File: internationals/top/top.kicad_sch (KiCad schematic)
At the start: 19 parts, among them J1 Conn_01x08_Pin, J2 Pico-L-Headerx5, J3 Pico-Debug-Headerx3, J4 Pico-R-Headerx5, J5 Bottom-UART-XHx2, J6 IMU-UART-XHx2, J7 Conn_01x03_Pin, J8 IMU-I2C0-XHx2, J9 IMU-I2C1-XHx2, M1 MotorDriver1A-XH-B4B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

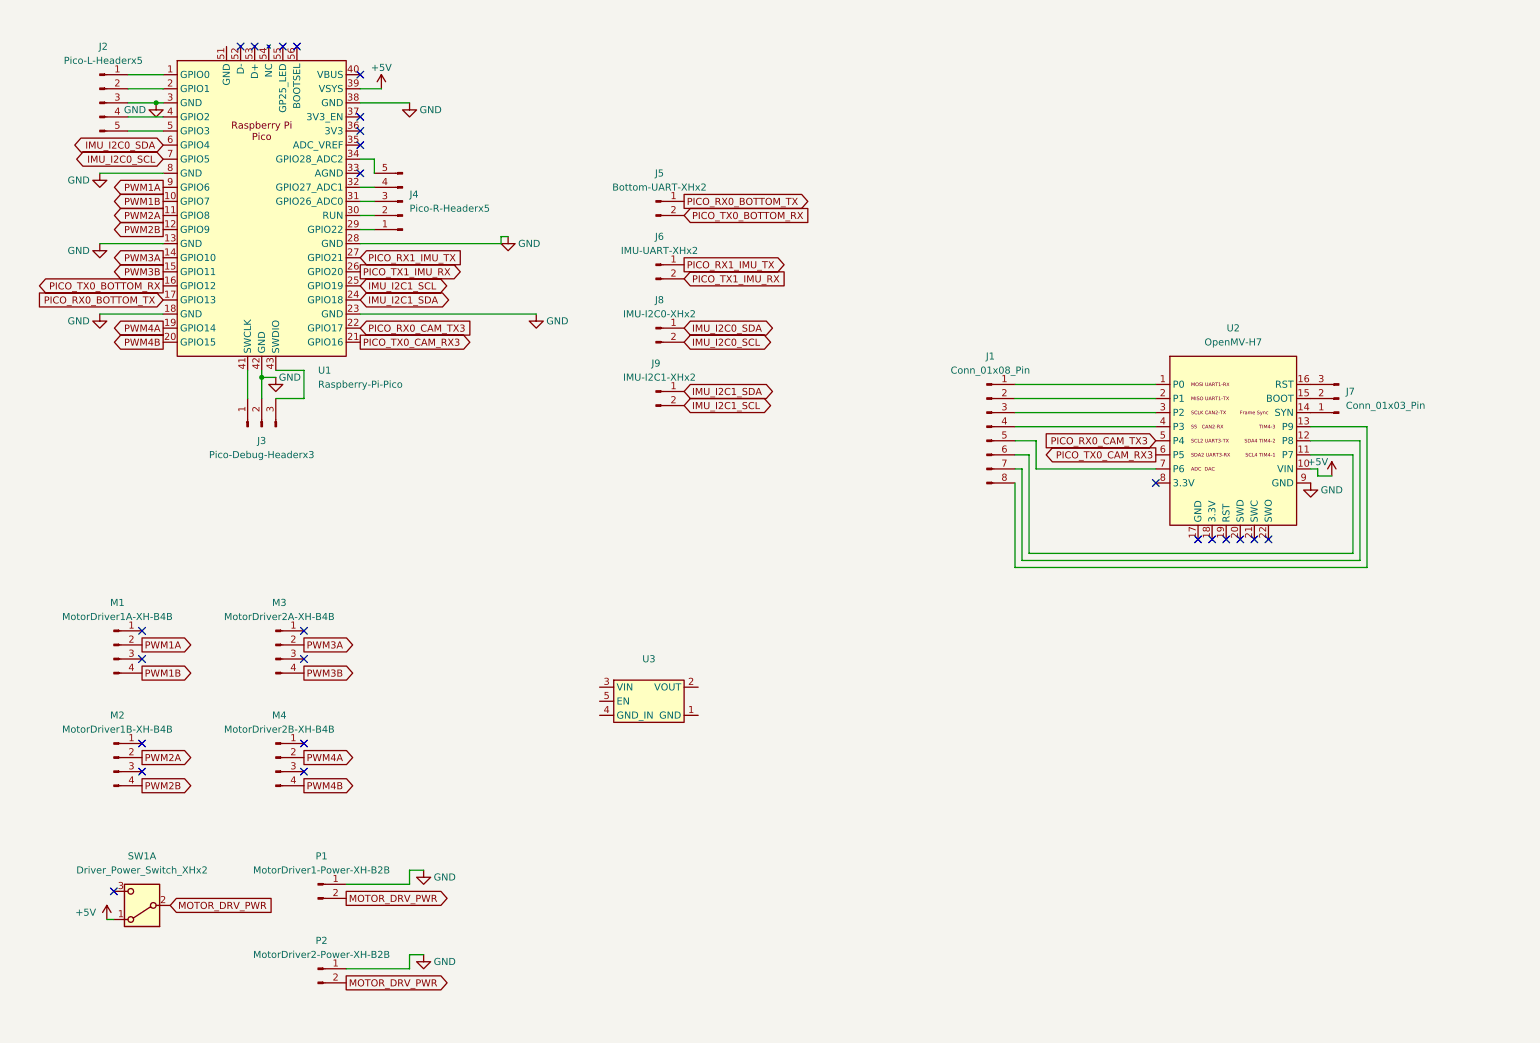
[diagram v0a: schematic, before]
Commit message: pcbs: top: feat: updated schematics
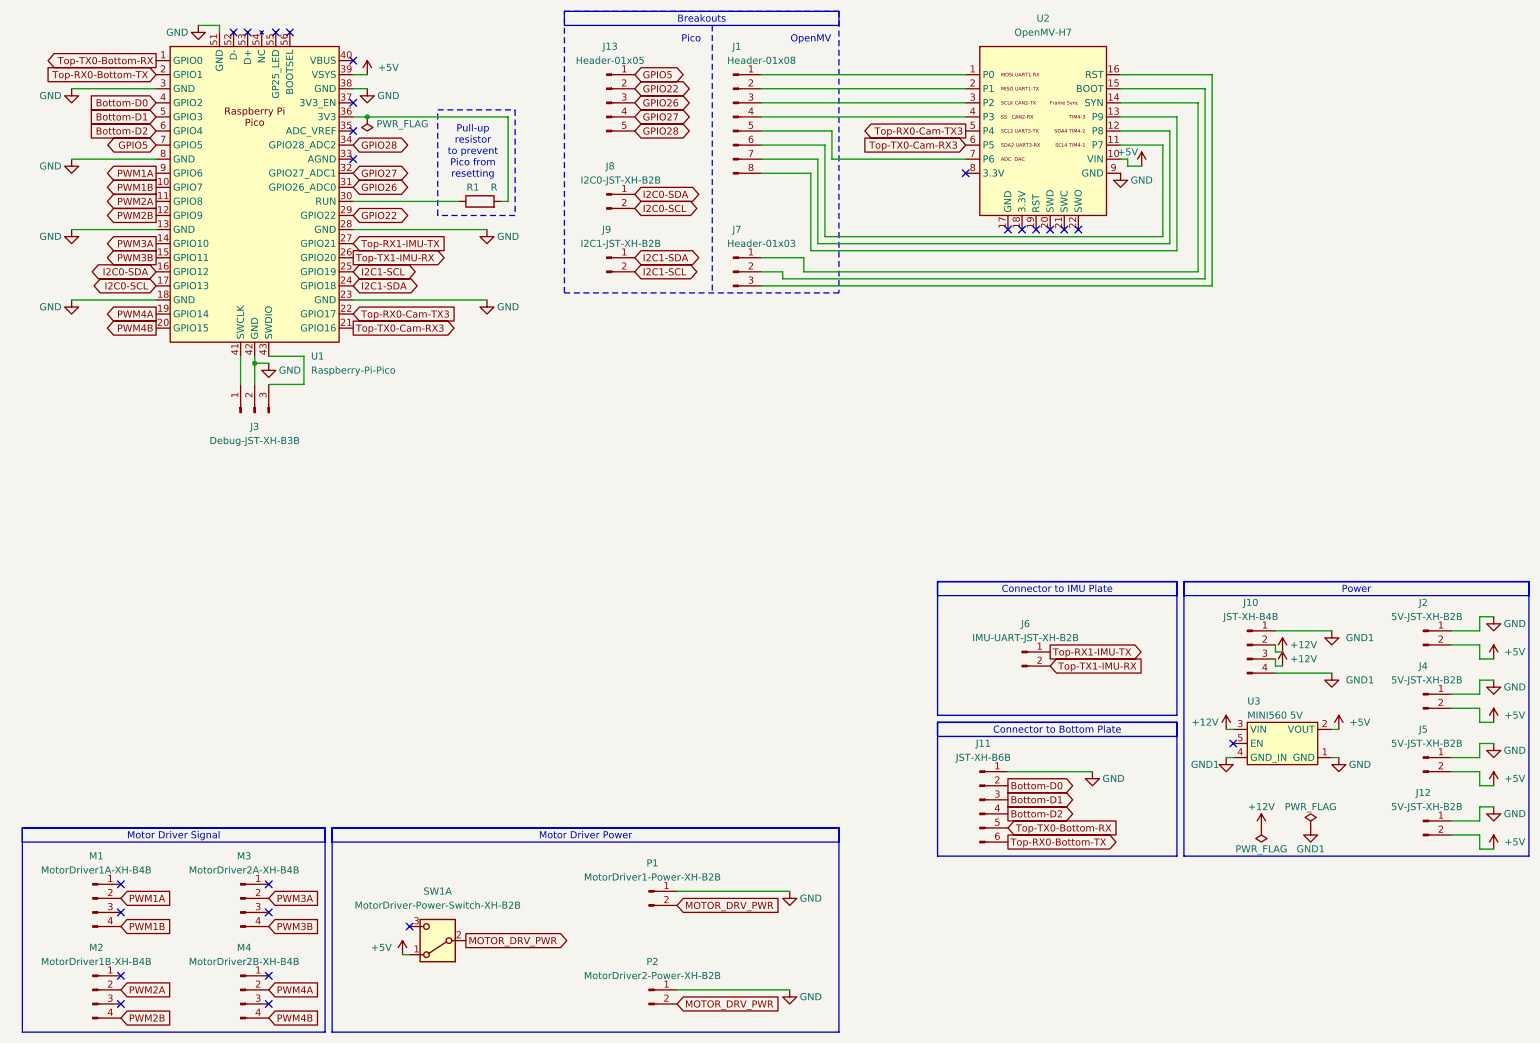
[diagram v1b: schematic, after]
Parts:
- removed J2: Pico-L-Headerx5, Connector_PinHeader_2.54mm:PinHeader_1x05_P2.54mm_Vertical, symbol Connector:Conn_01x05_Pin
- removed J4: Pico-R-Headerx5, Connector_PinHeader_2.54mm:PinHeader_1x05_P2.54mm_Vertical, symbol Connector:Conn_01x05_Pin
- added J10: JST-XH-B4B, Connector_JST:JST_XH_B4B-XH-A_1x04_P2.50mm_Vertical, symbol Connector:Conn_01x04_Pin
- added J11: JST-XH-B6B, Connector_JST:JST_XH_B6B-XH-A_1x06_P2.50mm_Vertical, symbol Connector:Conn_01x06_Pin
- added J12, J2, J4: 5V-JST-XH-B2B, Connector_JST:JST_XH_B2B-XH-A_1x02_P2.50mm_Vertical, symbol Connector:Conn_01x02_Pin
- added J13: Header-01x05, Connector_PinHeader_2.54mm:PinHeader_1x05_P2.54mm_Vertical, symbol Connector:Conn_01x05_Pin
- added R1: R, PCM_Resistor_THT_AKL:R_Axial_DIN0204_L3.6mm_D1.6mm_P5.08mm_Horizontal, symbol Device:R
- J1: value Conn_01x08_Pin -> Header-01x08; footprint (none) -> Connector_PinHeader_2.54mm:PinHeader_1x08_P2.54mm_Vertical
- J3: value Pico-Debug-Headerx3 -> Debug-JST-XH-B3B; footprint Connector_PinHeader_2.54mm:PinHeader_1x03_P2.54mm_Vertical -> Connector_JST:JST_XH_B3B-XH-A_1x03_P2.50mm_Vertical
- J5: value Bottom-UART-XHx2 -> 5V-JST-XH-B2B
- J6: value IMU-UART-XHx2 -> IMU-UART-JST-XH-B2B
- J7: value Conn_01x03_Pin -> Header-01x03; footprint (none) -> Connector_PinHeader_2.54mm:PinHeader_1x03_P2.54mm_Vertical
- J8: value IMU-I2C0-XHx2 -> I2C0-JST-XH-B2B
- J9: value IMU-I2C1-XHx2 -> I2C1-JST-XH-B2B
- SW1: value Driver_Power_Switch_XHx2 -> MotorDriver-Power-Switch-XH-B2B
- U3: value ~ -> MINI560 5V; footprint (none) -> PorridgePi-Personal:MINI560
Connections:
- net +5V: now also J5.2 (Pin_2), U3.2 (VOUT), J12.2 (Pin_2), J2.2 (Pin_2), J4.2 (Pin_2)
- net GND: now also J5.1 (Pin_1), U1.51 (GND), U3.1 (GND), J11.1 (Pin_1), J12.1 (Pin_1), J2.1 (Pin_1), J4.1 (Pin_1)
- net GPIO22: now reaches U1.29 (GPIO22)
- net GPIO22: now also J13.2 (Pin_2)
- net at U1.30 (RUN): now also R1.1
- net GPIO26: now reaches U1.31 (GPIO26_ADC0)
- net GPIO26: now also J13.3 (Pin_3)
- net GPIO27: now reaches U1.32 (GPIO27_ADC1)
- net GPIO27: now also J13.4 (Pin_4)
- net GPIO28: now reaches U1.34 (GPIO28_ADC2)
- net GPIO28: now also J13.5 (Pin_5)
- net +12V: now reaches U3.3 (VIN)
- net +12V: now also J10.2 (Pin_2), J10.3 (Pin_3)
- net GND1: now reaches U3.4 (GND_IN)
- net GND1: now also J10.1 (Pin_1), J10.4 (Pin_4)
- net Top-TX0-Bottom-RX: now reaches U1.1 (GPIO0)
- net Top-TX0-Bottom-RX: now also J11.5 (Pin_5)
- net Top-RX0-Bottom-TX: now reaches U1.2 (GPIO1)
- net Top-RX0-Bottom-TX: now also J11.6 (Pin_6)
- net at U1.36 (3V3): now also R1.2
- net Bottom-D0: now reaches U1.4 (GPIO2)
- net Bottom-D0: now also J11.2 (Pin_2)
- net Bottom-D1: now reaches U1.5 (GPIO3)
- net Bottom-D1: now also J11.3 (Pin_3)
- net IMU_I2C0_SCL renamed GPIO5
- net GPIO5: now also J13.1 (Pin_1); no longer J8.2 (Pin_2)
- net IMU_I2C0_SDA renamed Bottom-D2
- net Bottom-D2: now also J11.4 (Pin_4); no longer J8.1 (Pin_1)
- net IMU_I2C1_SCL renamed I2C1-SCL
- net IMU_I2C1_SDA renamed I2C1-SDA
- net PICO_RX0_BOTTOM_TX renamed I2C0-SCL
- net I2C0-SCL: now also J8.2 (Pin_2); no longer J5.1 (Pin_1)
- net PICO_RX0_CAM_TX3 renamed Top-RX0-Cam-TX3
- net PICO_RX1_IMU_TX renamed Top-RX1-IMU-TX
- net PICO_TX0_BOTTOM_RX renamed I2C0-SDA
- net I2C0-SDA: now also J8.1 (Pin_1); no longer J5.2 (Pin_2)
- net PICO_TX0_CAM_RX3 renamed Top-TX0-Cam-RX3
- net PICO_TX1_IMU_RX renamed Top-TX1-IMU-RX
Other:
- note added: "OpenMV"
- note added: "Pico"
- note added: "Pull-up resistor to prevent Pico from resetting"
- moved on the sheet: J1, J6, J8, J9, M1, M2, M3, M4, P1, P2, SW1A, U1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

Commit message: pcbs: top: feat: add buttons
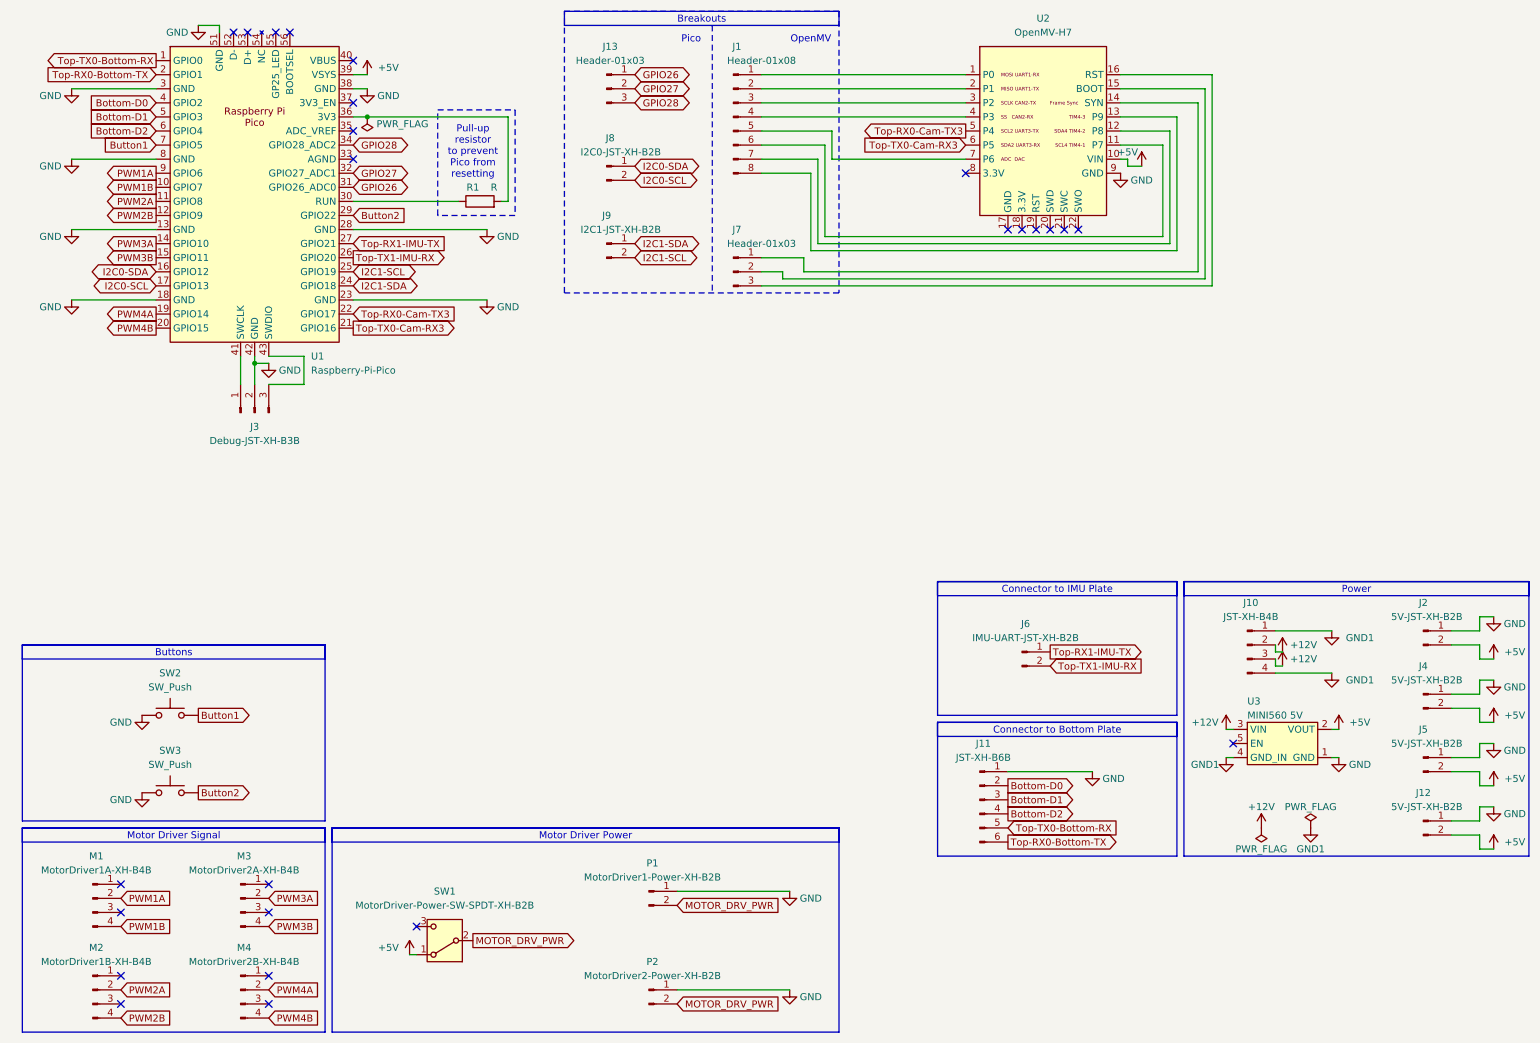
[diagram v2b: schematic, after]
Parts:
- removed J13: Header-01x05, Connector_PinHeader_2.54mm:PinHeader_1x05_P2.54mm_Vertical, symbol Connector:Conn_01x05_Pin
- removed SW1: MotorDriver-Power-Switch-XH-B2B, Connector_JST:JST_XH_B2B-XH-A_1x02_P2.50mm_Vertical, symbol Switch:SW_DPDT_x2
- added J13: Header-01x03, symbol Connector:Conn_01x03_Pin
- added SW1: MotorDriver-Power-SW-SPDT-XH-B2B, Connector_JST:JST_XH_B2B-XH-A_1x02_P2.50mm_Vertical, symbol Switch:SW_SPDT
- added SW2, SW3: SW_Push, Button_Switch_THT:SW_PUSH_6mm, symbol Switch:SW_Push
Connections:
- net +5V: now also SW1.1 (A)
- net GND: now also SW2.1, SW3.1
- net GPIO26: now also J13.1 (Pin_1)
- net GPIO27: now also J13.2 (Pin_2)
- net GPIO28: now also J13.3 (Pin_3)
- net MOTOR_DRV_PWR: now also SW1.2 (B)
- net GPIO22 renamed Button2
- net Button2: now also SW3.2
- net GPIO5 renamed Button1
- net Button1: now also SW2.2
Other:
- moved on the sheet: J8, J9

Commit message: pcbs: top: fix: missing footprint in schematics
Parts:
- J13: footprint (none) -> Connector_PinHeader_2.54mm:PinHeader_1x03_P2.54mm_Vertical
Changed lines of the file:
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@@
 		(title "Top Plate")
 		(date "2024-06-08")
-		(rev "1.2.0")
+		(rev "1.2.1")
 		(company "Zhou Yikun & Zachary Ang")
 		(comment 1 "RoboCup Junior Soccer Open 2024")
@@
 			)
 		)
-		(property "Footprint" ""
+		(property "Footprint" "Connector_PinHeader_2.54mm:PinHeader_1x03_P2.54mm_Vertical"
 			(at 118.11 26.67 0)
 			(effects
